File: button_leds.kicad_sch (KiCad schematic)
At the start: 70 parts

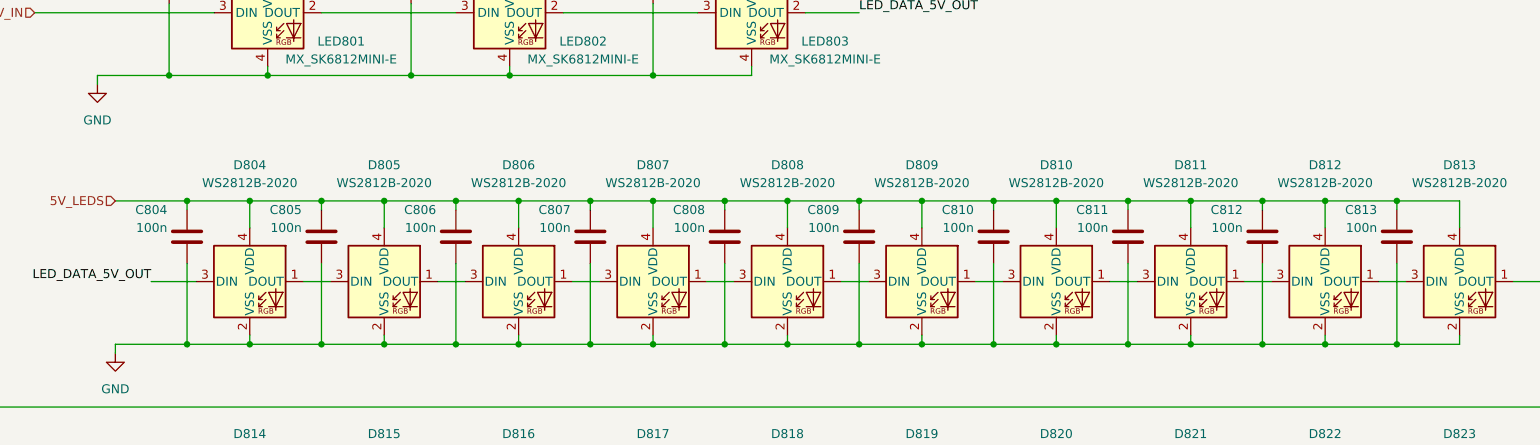
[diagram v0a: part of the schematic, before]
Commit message: Started adding LCSC part numbers to make ordering the parts easier
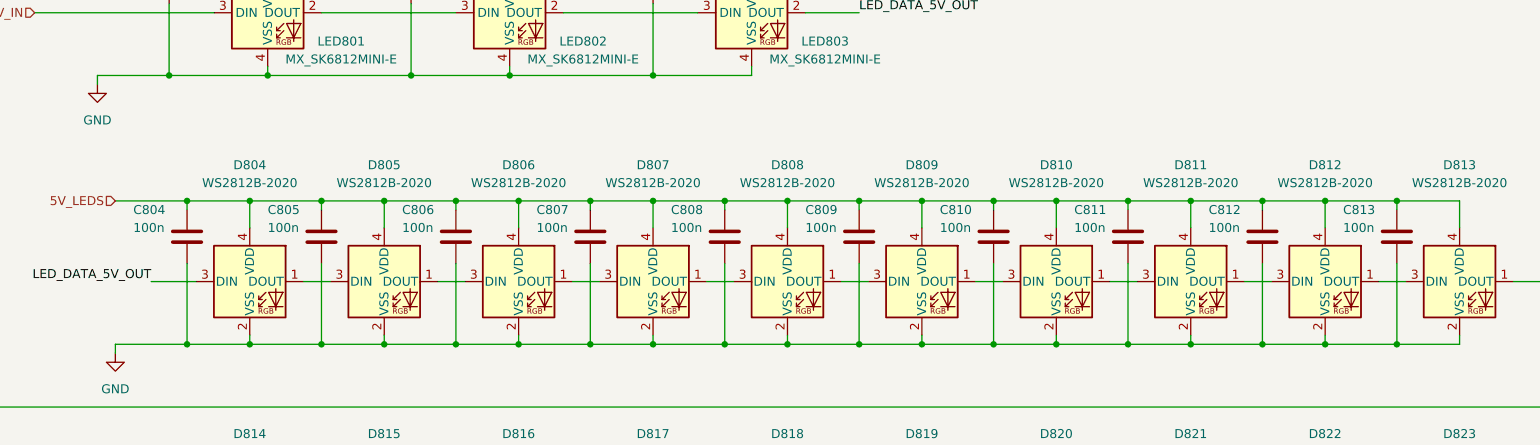
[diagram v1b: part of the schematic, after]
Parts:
- C801, C802, C803, C804, C805, C806, C807, C808, C809, C810, C811, C812, C813: LCSC (none) -> C42405541
